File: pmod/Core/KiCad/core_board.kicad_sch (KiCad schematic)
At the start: 23 parts, among them J1 USB_C_Receptacle_USB2.0_16P, Q1 L8080PLT1G, Q2 L8080PLT1G, SW1 SW, SW1_BOOT SW, U1 ESP32-S3-WROOM, U2 SGM2212-3.3XKC3G, U3 CP2102

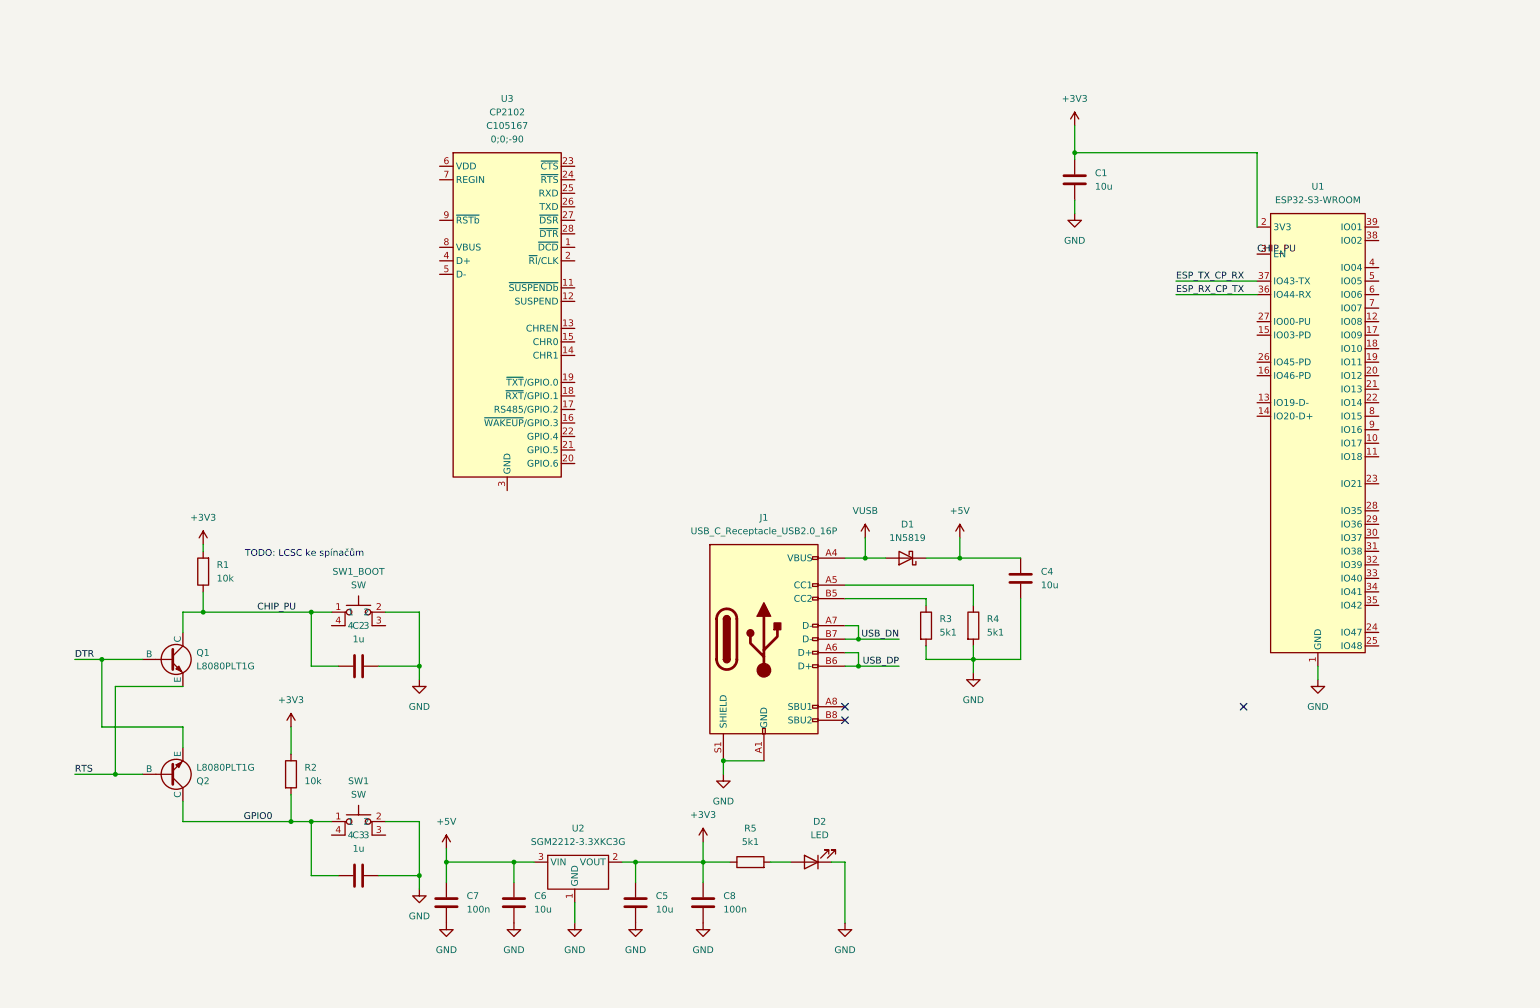
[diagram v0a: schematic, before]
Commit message: Routed board
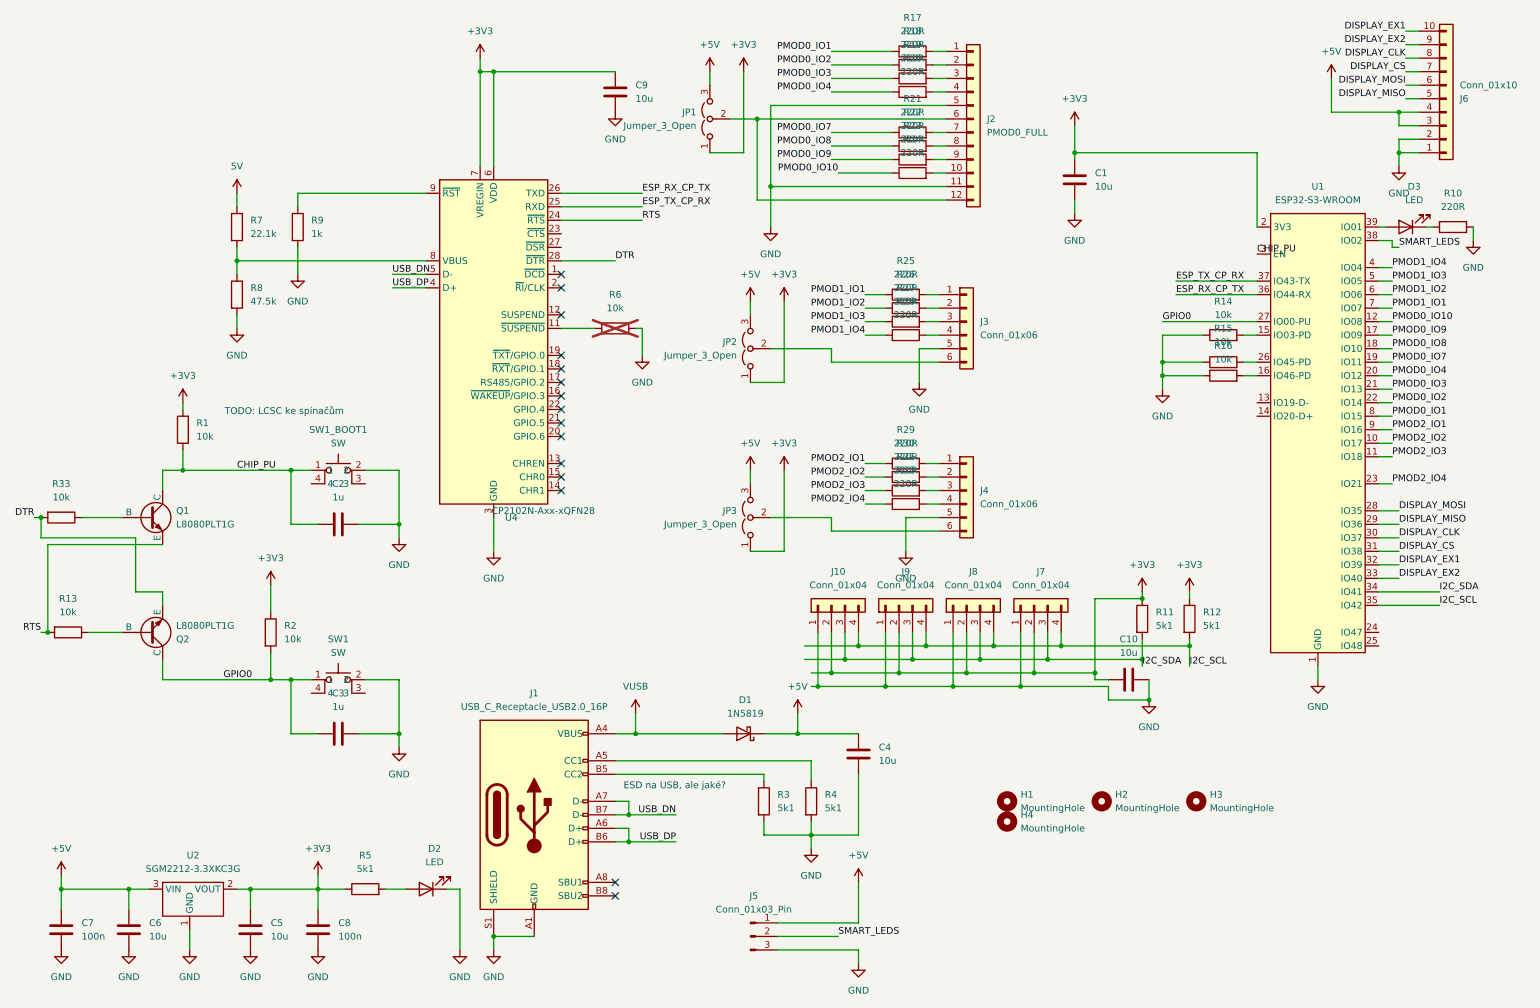
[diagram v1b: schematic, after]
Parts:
- removed U3: CP2102, Package_DFN_QFN:QFN-28-1EP_5x5mm_P0.5mm_EP3.35x3.35mm, symbol RKL-BusCnverters:CP2102
- added C10, C9: 10u, Capacitor_SMD:C_1206_3216Metric_Pad1.33x1.80mm_HandSolder, symbol Device:C
- added D3: LED, LED_SMD:LED_0603_1608Metric, symbol Device:LED
- added H1, H2, H3, H4: MountingHole, MountingHole:MountingHole_3.2mm_M3_DIN965, symbol Mechanical:MountingHole
- added J10, J7, J8, J9: Conn_01x04, Connector_JST:JST_SH_SM04B-SRSS-TB_1x04-1MP_P1.00mm_Horizontal, symbol Connector_Generic:Conn_01x04
- added J2: PMOD0_FULL, Conn_PMOD:PinSocket_PMOD_Full, symbol Connector_Generic:Conn_01x12
- added J3, J4: Conn_01x06, Conn_PMOD:PinSocket_PMOD_Half, symbol Connector_Generic:Conn_01x06
- added J5: Conn_01x03_Pin, Connector_PinHeader_2.54mm:PinHeader_1x03_P2.54mm_Horizontal, symbol Connector:Conn_01x03_Pin
- added J6: Conn_01x10, Connector_JST:JST_XH_S10B-XH-A-1_1x10_P2.50mm_Horizontal, symbol Connector_Generic:Conn_01x10
- added JP1, JP2, JP3: Jumper_3_Open, Connector_PinHeader_2.54mm:PinHeader_1x03_P2.54mm_Vertical, symbol Jumper:Jumper_3_Open
- added R10, R17, R18, R19, R20, R21, R22, R23, R24, R25, R26, R27, R28, R29, R30, R31, R32: 220R, Resistor_SMD:R_0402_1005Metric, symbol Device:R
- added R11, R12: 5k1, Resistor_SMD:R_0603_1608Metric, symbol Device:R
- added R13, R14, R15, R16, R33, R6: 10k, Resistor_SMD:R_0603_1608Metric, symbol Device:R
- added R7: 22.1k, Resistor_SMD:R_0603_1608Metric, symbol Device:R
- added R8: 47.5k, Resistor_SMD:R_0603_1608Metric, symbol Device:R
- added R9: 1k, Resistor_SMD:R_0603_1608Metric, symbol Device:R
- added U4: CP2102N-Axx-xQFN28, Package_DFN_QFN:QFN-28-1EP_5x5mm_P0.5mm_EP3.35x3.35mm, symbol Interface_USB:CP2102N-Axx-xQFN28
- SW1: footprint RLK-ElectorMechanicalComponents:Tactile_switch -> RKL-ElectroMechanicalComponents:Tactile_switch
- renumbered SW1_BOOT to SW1_BOOT1
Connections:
- net +3V3: now also C10.1, C9.1, J10.2 (Pin_2), J7.2 (Pin_2), J8.2 (Pin_2), J9.2 (Pin_2), JP1.1 (A), JP2.1 (A), JP3.1 (A), R11.1, R12.1, U4.6 (VDD), U4.7 (VREGIN)
- net +5V: now also J5.1 (Pin_1), J6.3 (Pin_3), J6.4 (Pin_4), JP1.3 (B), JP2.3 (B), JP3.3 (B)
- net DTR: now also R33.2, U4.28 (~{DTR}); no longer Q1.1 (B)
- net ESP_RX_CP_TX: now also U4.26 (TXD)
- net ESP_TX_CP_RX: now also U4.25 (RXD)
- net GND: now also C10.2, C9.2, J10.1 (Pin_1), J2.11 (Pin_11), J2.5 (Pin_5), J3.5 (Pin_5), J4.5 (Pin_5), J5.3 (Pin_3), J6.1 (Pin_1), J6.2 (Pin_2), J7.1 (Pin_1), J8.1 (Pin_1), J9.1 (Pin_1), R10.2, R14.1, R15.1, R16.1, R6.2, R8.2, R9.2, U4.29 (GND), U4.3 (GND)
- net GPIO0: now also U1.27 (IO00-PU)
- net RTS: now also R13.2, U4.24 (~{RTS}); no longer Q2.1 (B)
- net USB_DN: now also U4.5 (D-)
- net USB_DP: now also U4.4 (D+)
- net PMOD2_IO2: now reaches U1.10 (IO17)
- net PMOD2_IO2: now also R30.1
- net PMOD2_IO3: now reaches U1.11 (IO18)
- net PMOD2_IO3: now also R31.1
- net PMOD0_IO10: now reaches U1.12 (IO08)
- net PMOD0_IO10: now also R24.1
- net at U1.15 (IO03-PD): now also R14.2
- net at U1.16 (IO46-PD): now also R16.2
- net PMOD0_IO9: now reaches U1.17 (IO09)
- net PMOD0_IO9: now also R23.1
- net PMOD0_IO8: now reaches U1.18 (IO10)
- net PMOD0_IO8: now also R22.1
- net PMOD0_IO7: now reaches U1.19 (IO11)
- net PMOD0_IO7: now also R21.1
- net PMOD0_IO4: now reaches U1.20 (IO12)
- net PMOD0_IO4: now also R20.1
- net PMOD0_IO3: now reaches U1.21 (IO13)
- net PMOD0_IO3: now also R19.1
- net PMOD0_IO2: now reaches U1.22 (IO14)
- net PMOD0_IO2: now also R18.1
- net PMOD2_IO4: now reaches U1.23 (IO21)
- net PMOD2_IO4: now also R32.1
- net at U1.26 (IO45-PD): now also R15.2
- net DISPLAY_MOSI: now reaches U1.28 (IO35)
- net DISPLAY_MOSI: now also J6.6 (Pin_6)
- net DISPLAY_MISO: now reaches U1.29 (IO36)
- net DISPLAY_MISO: now also J6.5 (Pin_5)
- net DISPLAY_CLK: now reaches U1.30 (IO37)
- net DISPLAY_CLK: now also J6.8 (Pin_8)
- net DISPLAY_CS: now reaches U1.31 (IO38)
- net DISPLAY_CS: now also J6.7 (Pin_7)
- net DISPLAY_EX1: now reaches U1.32 (IO39)
- net DISPLAY_EX1: now also J6.10 (Pin_10)
- net DISPLAY_EX2: now reaches U1.33 (IO40)
- net DISPLAY_EX2: now also J6.9 (Pin_9)
- net I2C_SDA: now reaches U1.34 (IO41)
- net I2C_SDA: now also J10.3 (Pin_3), J7.3 (Pin_3), J8.3 (Pin_3), J9.3 (Pin_3), R11.2
- net I2C_SCL: now reaches U1.35 (IO42)
- net I2C_SCL: now also J10.4 (Pin_4), J7.4 (Pin_4), J8.4 (Pin_4), J9.4 (Pin_4), R12.2
- net SMART_LEDS: now reaches U1.38 (IO02)
- net SMART_LEDS: now also J5.2 (Pin_2)
- net at U1.39 (IO01): now also D3.2 (A)
- net PMOD1_IO4: now reaches U1.4 (IO04)
- net PMOD1_IO4: now also R28.1
- net PMOD1_IO3: now reaches U1.5 (IO05)
- net PMOD1_IO3: now also R27.1
- net PMOD1_IO2: now reaches U1.6 (IO06)
- net PMOD1_IO2: now also R26.1
- net PMOD1_IO1: now reaches U1.7 (IO07)
- net PMOD1_IO1: now also R25.1
- net PMOD0_IO1: now reaches U1.8 (IO15)
- net PMOD0_IO1: now also R17.1
- net PMOD2_IO1: now reaches U1.9 (IO16)
- net PMOD2_IO1: now also R29.1
- new net: J3.3 (Pin_3), R27.2
- new net: J4.6 (Pin_6), JP3.2 (C)
- new net: J2.3 (Pin_3), R19.2
- new net: J2.1 (Pin_1), R17.2
- new net: R7.2, R8.1, U4.8 (VBUS)
- new net: Q1.1 (B), R33.1
- new net: R6.1, U4.11 (~{SUSPEND})
- new net: R9.1, U4.9 (~{RST})
- new net: J2.2 (Pin_2), R18.2
- new net: J3.4 (Pin_4), R28.2
- new net: J2.7 (Pin_7), R21.2
- new net: J4.2 (Pin_2), R30.2
- new net: J2.9 (Pin_9), R23.2
- new net: J4.3 (Pin_3), R31.2
- new net: J3.6 (Pin_6), JP2.2 (C)
- new net: J4.4 (Pin_4), R32.2
- new net: D3.1 (K), R10.1
- new net: J3.2 (Pin_2), R26.2
- new net: J3.1 (Pin_1), R25.2
- new net: J2.8 (Pin_8), R22.2
- new net: Q2.1 (B), R13.1
- new net: J4.1 (Pin_1), R29.2
- new net: J2.12 (Pin_12), J2.6 (Pin_6), JP1.2 (C)
- new net: J2.10 (Pin_10), R24.2
- new net: J2.4 (Pin_4), R20.2
- new net 5V: R7.1
- no-connect marks 3 -> 15
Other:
- note added: "ESD na USB, ale jaké?"
- moved on the sheet: C2, C3, C4, C5, C6, C7, C8, D1, D2, J1, Q1, Q2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

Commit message: Multiple changes (dzarda):
odstraněna VBUS dioda
přidán microUSB
použit CH340 z Robutka
USB ESD
separovány I2C, 2x2 uŠupy
uŠupy vyvedeny také na pinhead díry
změněn display pinout, rozmístění GND, odpojen jeden EX pin
přidáno trochu filtrování v napájení displaye
přidány 100R rezistory na IO
přidány 100nF k IO portům
změna na 0402
umožněno použití 8MB Octal PSRAM
odstraněna gpio stupid LED
přidána smart LED + výstup na LED pásek (jak na Robutkovi)
zmenšeny rozměry DPS
poházeny pinouty GPIO pro lepší layout
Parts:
- removed C2: 1u, Capacitor_SMD:C_1206_3216Metric_Pad1.33x1.80mm_HandSolder, symbol Device:C
- removed D1: 1N5819, Diode_THT:D_DO-41_SOD81_P10.16mm_Horizontal, symbol Diode:1N5819
- removed D3: LED, LED_SMD:LED_0603_1608Metric, symbol Device:LED
- removed J1: USB_C_Receptacle_USB2.0_16P, Connector_USB:USB_C_Receptacle_HRO_TYPE-C-31-M-12, symbol Connector:USB_C_Receptacle_USB2.0_16P
- removed J5: Conn_01x03_Pin, Connector_PinHeader_2.54mm:PinHeader_1x03_P2.54mm_Horizontal, symbol Connector:Conn_01x03_Pin
- removed Q1, Q2: L8080PLT1G, Package_TO_SOT_SMD:SOT-23, symbol PMOD_Core_Beans:L8080PLT1G
- removed R10, R17, R18, R19, R20, R21, R22, R23, R24, R25, R26, R27, R28, R29, R30, R31, R32: 220R, Resistor_SMD:R_0402_1005Metric, symbol Device:R
- removed R11, R12: 5k1, Resistor_SMD:R_0603_1608Metric, symbol Device:R
- removed R13: 10k, Resistor_SMD:R_0603_1608Metric, symbol Device:R
- removed SW1, SW1_BOOT1: SW, RKL-ElectroMechanicalComponents:Tactile_switch, symbol RKL-Uncategorized:SW
- removed U4: CP2102N-Axx-xQFN28, Package_DFN_QFN:QFN-28-1EP_5x5mm_P0.5mm_EP3.35x3.35mm, symbol Interface_USB:CP2102N-Axx-xQFN28
- added C11, C12, C13, C15, C16, C17, C18, C19, C20, C21, C22, C23: 100n, Capacitor_SMD:C_0402_1005Metric, symbol Device:C
- added C14: 100n, Capacitor_SMD:C_0402_1005Metric, symbol B.B-rescue:C-Device-B.B-rescue-B.B-rescue
- added C2: EEEFK1H470XP, Capacitor_SMD:CP_Elec_6.3x7.7, symbol Device:C_Polarized
- added D5: SMBJ6.5CA, Diode_SMD:D_SMB, symbol Diode:SMAJ5.0A
- added D6, D7, D8, D9: H3V3LD5B, Diode_SMD:D_SOD-523, symbol Diode:SMAJ5.0A
- added FB1: BLM18PG121SN1D, Inductor_SMD:L_0603_1608Metric, symbol Device:FerriteBead
- added J1, J14: Conn_01x04_Pin, Connector_PinSocket_2.54mm:PinSocket_1x04_P2.54mm_Vertical, symbol Connector:Conn_01x04_Pin
- added J11: USB_B_Micro, Connector_USB:USB_Micro-B_Molex-105017-0001, symbol Connector:USB_B_Micro
- added J12: USB_C_Receptacle_USB2.0, Connector_USB:USB_C_Receptacle_HRO_TYPE-C-31-M-12, symbol Connector:USB_C_Receptacle_USB2.0
- added J13: Conn_01x03, Connector_JST:JST_XH_S3B-XH-A-1_1x03_P2.50mm_Horizontal, symbol Connector_Generic:Conn_01x03
- added Q3, Q4: Q_NPN_BEC, Package_TO_SOT_SMD:SOT-23, symbol Device:Q_NPN_BEC
- added R34, R69, R70, R71: 5k1, Resistor_SMD:R_0402_1005Metric, symbol Device:R
- added R35, R36: 10k, Resistor_SMD:R_0402_1005Metric, symbol Device:R
- added R37, R38, R39, R40: 2k, Resistor_SMD:R_0402_1005Metric, symbol Device:R
- added RN1, RN2: 100R, Resistor_SMD:R_Array_Convex_4x0603, symbol Device:R_Pack04
- added RN3, RN4, RN5, RN6: 100R, Resistor_SMD:R_Array_Convex_4x0603, symbol Device:R_Pack04_Split
- added SW2: EN, Button_Switch_SMD:SW_Push_1P1T_NO_Vertical_Wuerth_434133025816, symbol Switch:SW_Push
- added SW3: BOOT, Button_Switch_SMD:SW_Push_1P1T_NO_Vertical_Wuerth_434133025816, symbol Switch:SW_Push
- added TP1: GND, Connector_PinHeader_2.54mm:PinHeader_1x01_P2.54mm_Vertical, symbol Connector:TestPoint
- added TP2: +5V, Connector_PinHeader_2.54mm:PinHeader_1x01_P2.54mm_Vertical, symbol Connector:TestPoint
- added TP3: +3V3, Connector_PinHeader_2.54mm:PinHeader_1x01_P2.54mm_Vertical, symbol Connector:TestPoint
- added U6: CH340X, Package_SO:MSOP-10_3x3mm_P0.5mm, symbol Interface_USB:CH340X
- added U9: WS2812B, LED_SMD:LED_WS2812B-2020_PLCC4_2.0x2.0mm, symbol RKL-Uncategorized:WS2812B
- C1, C4, C5, C6: footprint Capacitor_SMD:C_1206_3216Metric_Pad1.33x1.80mm_HandSolder -> Capacitor_SMD:C_1206_3216Metric
- C10: value 10u -> 100n; footprint Capacitor_SMD:C_1206_3216Metric_Pad1.33x1.80mm_HandSolder -> Capacitor_SMD:C_0402_1005Metric; LCSC C13585 -> C307331
- C3: value 1u -> 10u; footprint Capacitor_SMD:C_1206_3216Metric_Pad1.33x1.80mm_HandSolder -> Capacitor_SMD:C_1206_3216Metric; LCSC C13832 -> C13585
- C7, C8: footprint Capacitor_SMD:C_0603_1608Metric -> Capacitor_SMD:C_0402_1005Metric; LCSC C14663 -> C307331
- C9: value 10u -> 100n; footprint Capacitor_SMD:C_1206_3216Metric_Pad1.33x1.80mm_HandSolder -> Capacitor_SMD:C_0402_1005Metric; Basic/Extended (none) -> B; LCSC C13585 -> C307331; info (none) -> 16V, X7R
- D2: value LED -> RED
- J10, J7, J8, J9: symbol Connector_Generic:Conn_01x04 -> Connector_Generic_MountingPin:Conn_01x04_MountingPin
- R1, R14, R15, R16, R2: footprint Resistor_SMD:R_0603_1608Metric -> Resistor_SMD:R_0402_1005Metric; LCSC C98220 -> C25744
- R3: value 5k1 -> 4R7; footprint Resistor_SMD:R_0603_1608Metric -> Resistor_SMD:R_0805_2012Metric; LCSC C2907044 -> C17675
- R33: value 10k -> 100R; footprint Resistor_SMD:R_0603_1608Metric -> Resistor_SMD:R_0402_1005Metric; LCSC C98220 -> C25076
- R4: value 5k1 -> 100R; footprint Resistor_SMD:R_0603_1608Metric -> Resistor_SMD:R_0402_1005Metric; LCSC C2907044 -> C25076
- R5: footprint Resistor_SMD:R_0603_1608Metric -> Resistor_SMD:R_0402_1005Metric; LCSC C2907044 -> C25905
- R6: value 10k -> 100R; footprint Resistor_SMD:R_0603_1608Metric -> Resistor_SMD:R_0402_1005Metric; LCSC C98220 -> C25076; now fitted
- R7: value 22.1k -> 100R; footprint Resistor_SMD:R_0603_1608Metric -> Resistor_SMD:R_0402_1005Metric; LCSC C25961 -> C25076
- R8: value 47.5k -> 100R; footprint Resistor_SMD:R_0603_1608Metric -> Resistor_SMD:R_0402_1005Metric; LCSC C23061 -> C25076
- R9: value 1k -> 100R; footprint Resistor_SMD:R_0603_1608Metric -> Resistor_SMD:R_0402_1005Metric; LCSC C22548 -> C25076
- U1: value ESP32-S3-WROOM -> ESP32-S3-WROOM-1-N16R8; LCSC C3013946 -> C2913202
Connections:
- net +3V3: now also C11.1, C12.1, C13.1, C14.1, C15.1, C20.1, J1.3 (Pin_3), J14.3 (Pin_3), R37.2, R38.2, R39.2, R40.2, TP3.1, U6.10 (V3), U6.7 (VCC); no longer C10.1, C9.1
- net +5V: now also C10.1, R9.2, C16.1, C19.1, C2.1, D5.1 (A1), FB1.1, J11.1 (VBUS), J12.A4 (VBUS), J12.A9 (VBUS), J12.B4 (VBUS), J12.B9 (VBUS), J13.3 (Pin_3), TP2.1, U9.4 (VDD); no longer J6.3 (Pin_3), J6.4 (Pin_4)
- net DISPLAY_CLK: now also U1.35 (IO42), RN6.7 (R2.2), RN6.8 (R1.2); no longer J6.8 (Pin_8), U1.30 (IO37)
- net DISPLAY_CS: now also U1.34 (IO41), RN5.6 (R3.2); no longer J6.7 (Pin_7), U1.31 (IO38)
- net DISPLAY_EX1: now also U1.39 (IO01), RN6.6 (R3.2); no longer J6.10 (Pin_10), U1.32 (IO39)
- net DISPLAY_MISO: now also U1.31 (IO38), RN5.8 (R1.2); no longer J6.5 (Pin_5), U1.29 (IO36)
- net DISPLAY_MOSI: now also U1.32 (IO39), RN5.7 (R2.2); no longer J6.6 (Pin_6), U1.28 (IO35)
- net ESP_RX_CP_TX: now also U6.8 (TXD)
- net ESP_TX_CP_RX: now also U6.9 (RXD)
- net GND: now also J10.MP (MountPin), J6.8 (Pin_8), J7.MP (MountPin), J8.MP (MountPin), J9.MP (MountPin), C11.2, C12.2, C13.2, C14.2, C15.2, C16.2, C17.2, C18.2, C19.2, C2.2, C20.2, C21.2, C22.2, C23.2, D5.2 (A2), D6.2 (A2), D7.2 (A2), D8.2 (A2), D9.2 (A2), J1.4 (Pin_4), J11.5 (GND), J12.A1 (GND), J12.A12 (GND), J12.B1 (GND), J12.B12 (GND), J12.S1 (SHIELD), J13.1 (Pin_1), J14.4 (Pin_4), R69.2, R70.2, R71.2, SW2.2, SW3.2, TP1.1, U6.3 (GND), U9.2 (VSS); no longer J6.2 (Pin_2), R3.2, R4.2, R6.2, R8.2, R9.2
- net PMOD0_IO1: now also U1.21 (IO13), RN3.5 (R4.2); no longer U1.8 (IO15)
- net PMOD0_IO10: now also U1.8 (IO15), RN4.8 (R1.2); no longer U1.12 (IO08)
- net PMOD0_IO2: now also U1.19 (IO11), RN3.7 (R2.2); no longer U1.22 (IO14)
- net PMOD0_IO3: now also U1.11 (IO18), RN4.5 (R4.2); no longer U1.21 (IO13)
- net PMOD0_IO4: now also U1.9 (IO16), RN4.7 (R2.2); no longer U1.20 (IO12)
- net PMOD0_IO7: now also U1.20 (IO12), RN3.6 (R3.2); no longer U1.19 (IO11)
- net PMOD0_IO8: now also RN3.8 (R1.2)
- net PMOD0_IO9: now also U1.10 (IO17), RN4.6 (R3.2); no longer U1.17 (IO09)
- net PMOD1_IO1: now also RN1.5 (R4.2)
- net PMOD1_IO2: now also RN1.6 (R3.2)
- net PMOD1_IO3: now also RN1.7 (R2.2)
- net PMOD1_IO4: now also RN1.8 (R1.2)
- net PMOD2_IO1: now also U1.33 (IO40), RN2.5 (R4.2); no longer U1.9 (IO16)
- net PMOD2_IO2: now also U1.25 (IO48), RN2.6 (R3.2); no longer U1.10 (IO17)
- net PMOD2_IO3: now also U1.24 (IO47), RN2.7 (R2.2); no longer U1.11 (IO18)
- net PMOD2_IO4: now also U1.38 (IO02), RN2.8 (R1.2); no longer U1.23 (IO21)
- net SMART_LEDS: now also R14.2, U1.15 (IO03-PD), U9.3 (DIN); no longer U1.38 (IO02)
- net at J3.3 (Pin_3): now also RN1.2 (R2.1)
- net at J4.6 (Pin_6), JP3.2 (C): now also C22.1
- net at J2.3 (Pin_3): now also RN4.4 (R4.1)
- net at J2.1 (Pin_1): now also RN3.4 (R4.1)
- net at R7.2: now also J7.4 (Pin_4), J8.4 (Pin_4), J14.1 (Pin_1), R38.1; no longer R8.1
- net at R33.1: now also U9.1 (DOUT)
- net I2C2_SCL: now reaches R4.1
- net I2C2_SCL: now also U1.23 (IO21)
- net at R3.1: now also C3.1
- net at R6.1: now also J10.3 (Pin_3), J9.3 (Pin_3), J1.2 (Pin_2), R39.1
- net DISPLAY_+5V: now reaches R9.1
- net DISPLAY_+5V: now also J6.2 (Pin_2), J6.3 (Pin_3), R3.2, C21.1, FB1.2
- net at J2.2 (Pin_2): now also RN3.2 (R2.1)
- net at J3.4 (Pin_4): now also RN1.1 (R1.1)
- net at J2.7 (Pin_7): now also RN3.3 (R3.1)
- net at J4.2 (Pin_2): now also RN2.3 (R3.1)
- net at J2.9 (Pin_9): now also RN4.3 (R3.1)
- net at J4.3 (Pin_3): now also RN2.2 (R2.1)
- net at J3.6 (Pin_6), JP2.2 (C): now also C23.1
- net at J4.4 (Pin_4): now also RN2.1 (R1.1)
- net at J3.2 (Pin_2): now also RN1.3 (R3.1)
- net USBMAIN_D-: now reaches U1.13 (IO19-D-)
- net USBMAIN_D-: now also D6.1 (A1), J12.A7 (D-), J12.B7 (D-)
- net USBMAIN_D+: now reaches U1.14 (IO20-D+)
- net USBMAIN_D+: now also D7.1 (A1), J12.A6 (D+), J12.B6 (D+)
- net at J3.1 (Pin_1): now also RN1.4 (R4.1)
- net at J2.8 (Pin_8): now also RN3.1 (R1.1)
- net at J4.1 (Pin_1): now also RN2.4 (R4.1)
- net at J2.12 (Pin_12), J2.6 (Pin_6), JP1.2 (C): now also C9.1
- net at J2.10 (Pin_10): now also RN4.1 (R1.1)
- net at J2.4 (Pin_4): now also RN4.2 (R2.1)
- net 5V renamed I2C1_SCL
- net I2C1_SCL: now also U1.12 (IO08)
- net CHIP_PU renamed EN
- net EN: now also R2.2, C17.1, Q3.3 (C), SW2.1; no longer R1.1
- net DISPLAY_EX2: no longer names the net of J6.9 (Pin_9)
- net DISPLAY_EX2: no longer U1.33 (IO40)
- net DTR: no longer names the net of R33.2
- net DTR: now also J13.2 (Pin_2)
- removed net GPIO0: C3.1, R2.2, U1.27 (IO00-PU)
- removed net I2C_SCL: J10.4 (Pin_4), J7.4 (Pin_4), J8.4 (Pin_4), J9.4 (Pin_4), U1.35 (IO42)
- removed net I2C_SDA: J10.3 (Pin_3), J7.3 (Pin_3), J8.3 (Pin_3), J9.3 (Pin_3), U1.34 (IO41)
- new net: J11.6 (Shield), R71.1
- new net: Q4.2 (E), R34.1, R35.2, U6.6 (TNOW/~{DTR})
- new net: R34.2, U6.5 (~{CTS})
- new net: Q3.1 (B), R35.1
- new net: J14.2 (Pin_2), J7.3 (Pin_3), J8.3 (Pin_3), R37.1, R8.1
- new net: Q3.2 (E), R36.2, U6.4 (~{RTS})
- new net: J1.1 (Pin_1), J10.4 (Pin_4), J9.4 (Pin_4), R4.2, R40.1
- new net: Q4.1 (B), R36.1
- new net: J6.4 (Pin_4), RN5.1 (R1.1)
- new net: J6.10 (Pin_10), RN6.3 (R3.1)
- new net: J6.5 (Pin_5), RN5.2 (R2.1)
- new net: J6.6 (Pin_6), RN5.3 (R3.1)
- new net: J6.7 (Pin_7), RN6.1 (R1.1), RN6.2 (R2.1)
- new net CC1: J12.A5 (CC1), R70.1
- new net CC2: J12.B5 (CC2), R69.1
- new net GPIO0/BOOT: C18.1, Q4.3 (C), R1.1, SW3.1, U1.27 (IO00-PU)
- new net I2C1_SDA: R8.2, U1.17 (IO09)
- new net I2C2_SDA: R6.2, U1.22 (IO14)
- new net USBAUX_D+: D8.1 (A1), J11.3 (D+), U6.1 (UD+)
- new net USBAUX_D-: D9.1 (A1), J11.2 (D-), U6.2 (UD-)
- no-connect marks 15 -> 7
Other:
- note added: "1A max."
- note added: "Analog capable pins: ESP IO01 - IO20 PMOD IO4 (and PMOD IO10) pins must be within this range"
- note added: "Buttons"
- note added: "LDO"
- note added: "Must be kept LOW at reset"
- note added: "PMODs"
- note added: "RES"
- note added: "RP-HUB Display"
- note added: "USB-C"
- note added: "USB-UART converter"
- note added: "USB-micro"
- note added: "Unusable with 8MB Octal PSRAM (these 3 pins are shared with it)"
- note added: "WS2812B LED + Out"
- note added: "Změny oproti @Vigh verzi odstraněna VBUS dioda přidán microUSB použit CH340 z Robutka USB ESD separovány I2C, 2x2 uŠupy uŠupy vyvedeny také na pinhead díry změněn display pinout, rozmístění GND, odpojen jeden EX pin přidáno trochu filtrování v napájení displaye přidány 100R rezistory na IO přidány 100nF k IO portům změna na 0402 umožněno použití 8MB Octal PSRAM odstraněna gpio stupid LED přidána 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"
- note added: "µŠups"
- note removed: "ESD na USB, ale jaké?"
- note removed: "TODO: LCSC ke spínačům"
- moved on the sheet: C1, C4, C5, C6, C7, C8, D2, H1, H2, H3, H4, J2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

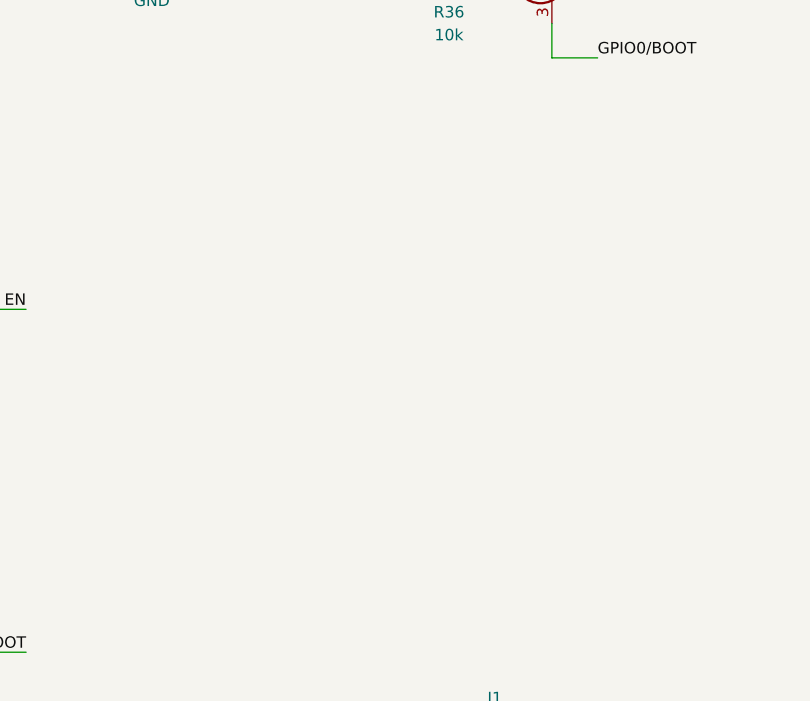
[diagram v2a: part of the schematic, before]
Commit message: Round corners and RX TX LEDs
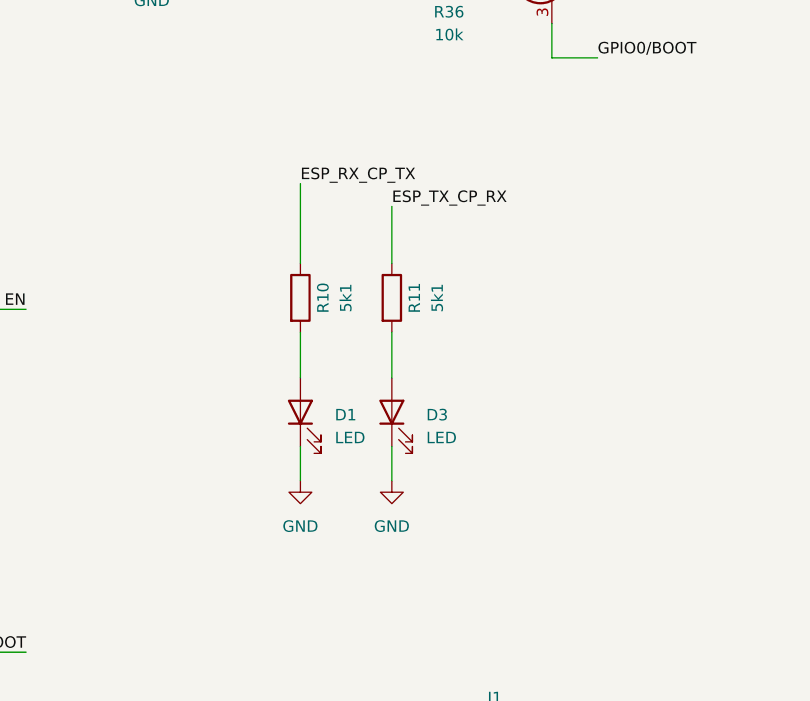
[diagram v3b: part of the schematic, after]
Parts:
- added D1, D3: LED, LED_SMD:LED_0402_1005Metric, symbol Device:LED
- added R10, R11: 5k1, Resistor_SMD:R_0402_1005Metric, symbol Device:R
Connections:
- net ESP_RX_CP_TX: now also R10.1
- net ESP_TX_CP_RX: now also R11.1
- net GND: now also D1.1 (K), D3.1 (K)
- new net: D1.2 (A), R10.2
- new net: D3.2 (A), R11.2
